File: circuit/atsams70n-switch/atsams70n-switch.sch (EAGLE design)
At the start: 70 parts, among them J5 CONN_20X2, Q1 20MHz, U1 REGULATOR_SOT223, U2 ATSAMS70N-TQFP100, U3 ISL3177E, U4 ISL3177E, U5 ISL3177E, U6 ISL3177E, X1 MICRO-USB_1/100

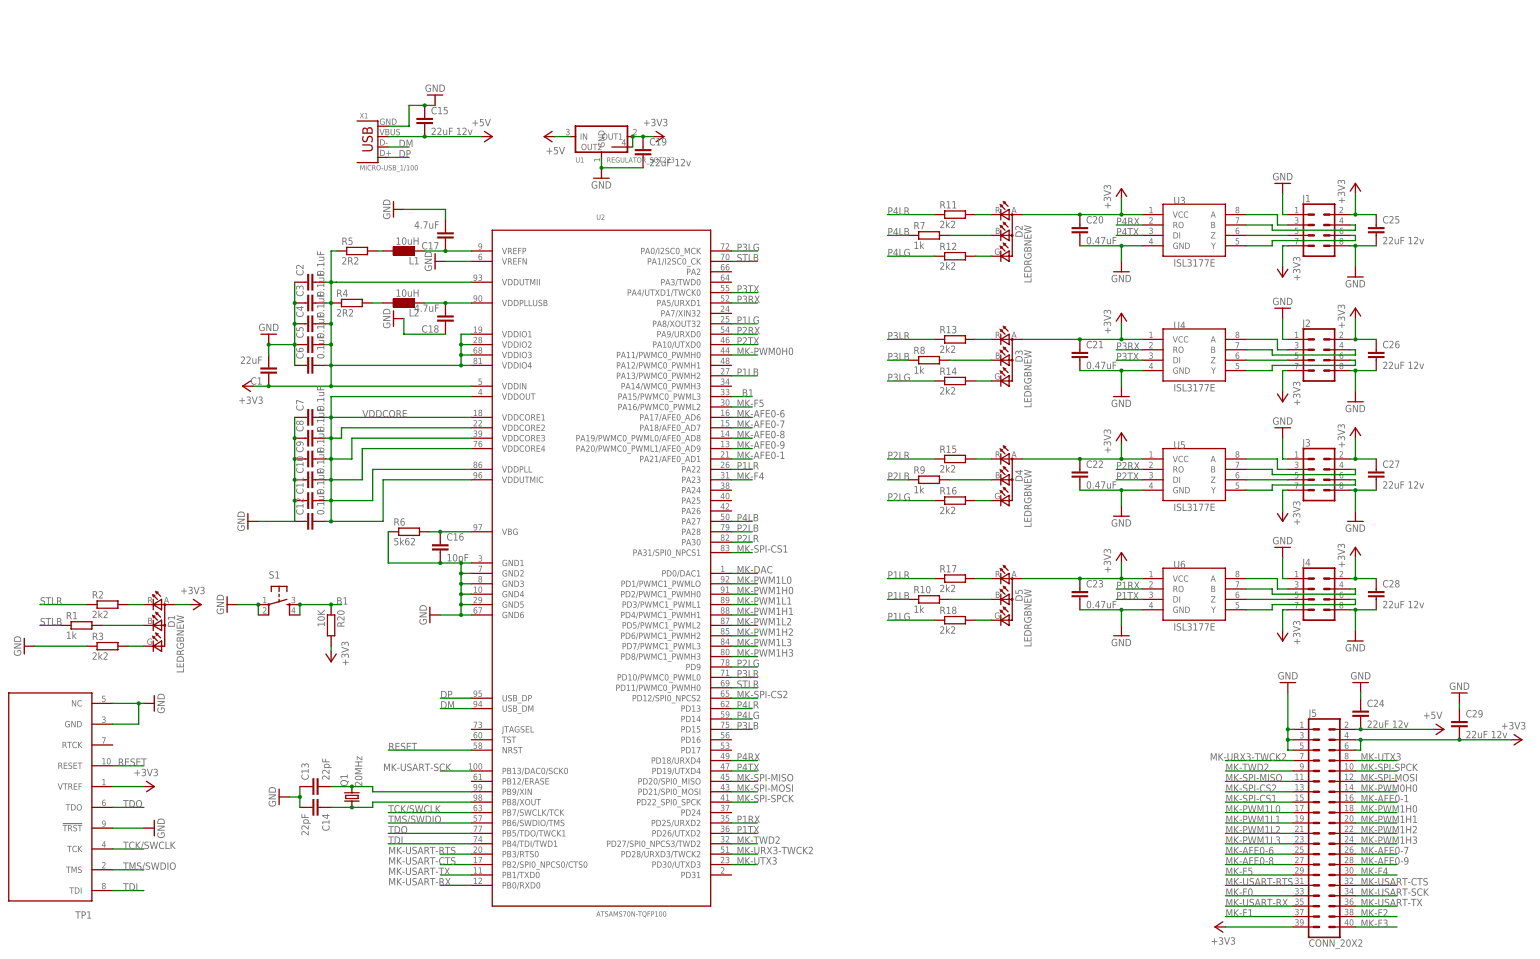
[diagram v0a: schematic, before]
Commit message: new boards to house
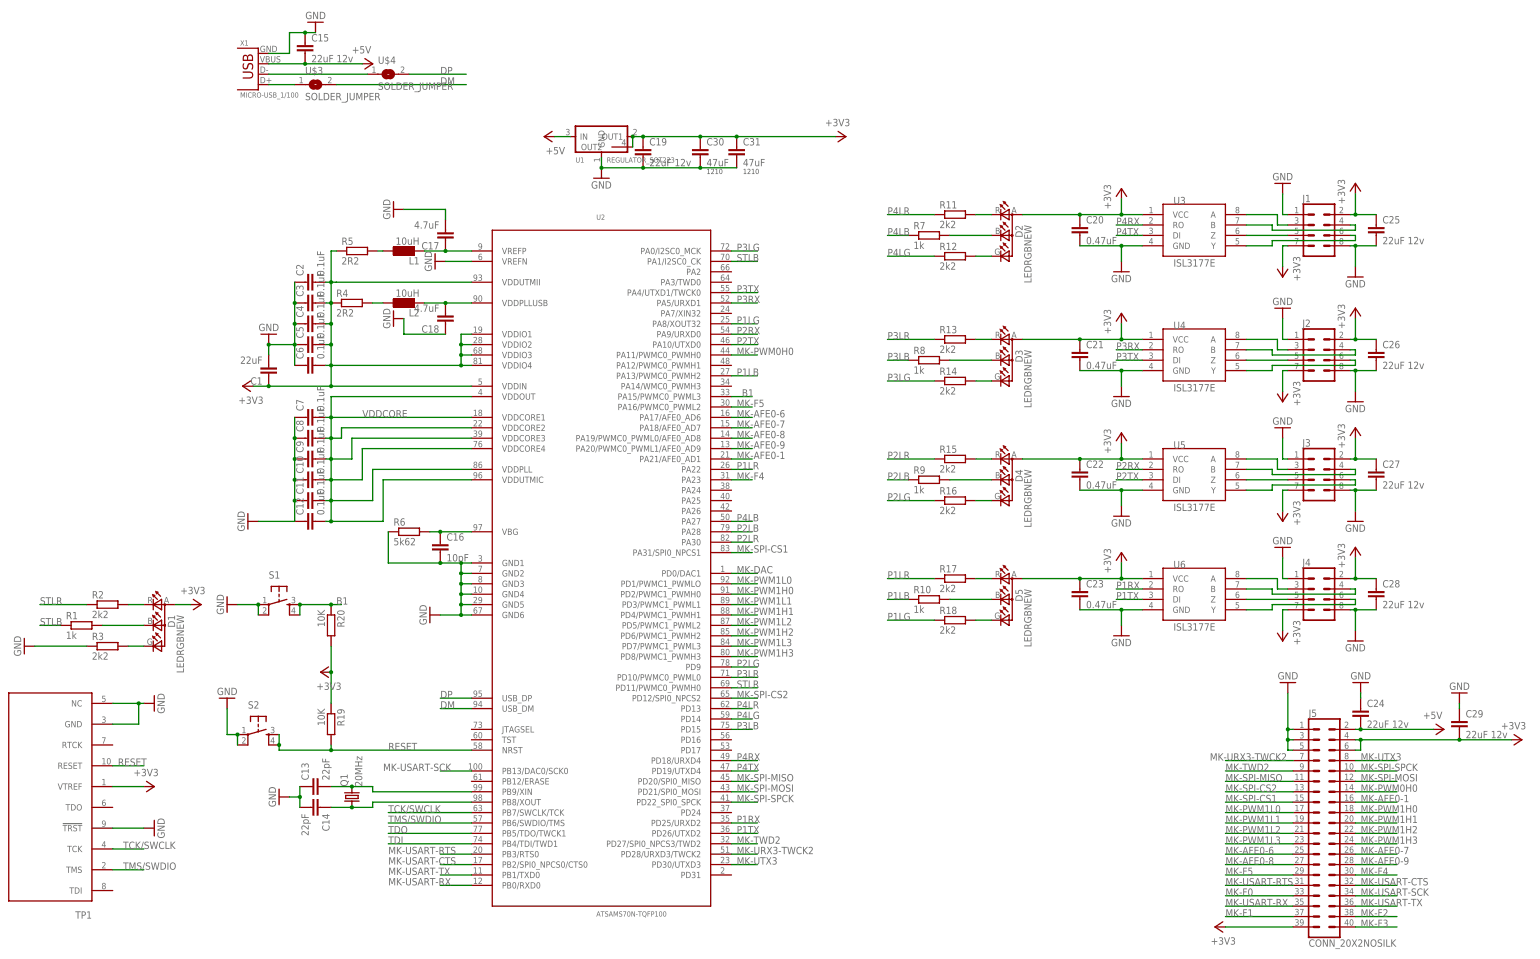
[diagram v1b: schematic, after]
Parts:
- added C30, C31: 47uF, borkedlabs-passives:CAP1210
- added R19: 10K, eagle-ltspice:R
- added S2: (no value), fab:6MM_SWITCH6MM_SWITCH
- added U$3, U$4: SOLDER_JUMPER, fab:SOLDER_JUMPER
- J5: value CONN_20X2 -> CONN_20X2NOSILK; device SparkFun-Connectors:CONN_20X2 -> SparkFun-Connectors:CONN_20X2NOSILK
- TP1: value TC2050-MCP-NL -> TC2050-NL; device tag-connect-2050:TC2050-MCP-NL -> tag-connect-2050:TC2050-NL
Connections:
- new net N$40: U$3.1, X1.D+
- new net N$6: U$4.1, X1.D-
- net +3V3: now also C30.1, C31.1, R19.1
- net DM: now also U$3.2; no longer X1.D-
- net DP: now also U$4.2; no longer X1.D+
- net GND: now also C30.2, C31.2, S2.P, S2.P1
- net RESET: now also R19.2, S2.S, S2.S1
- net TDI: no longer TP1.TDI
- net TDO: no longer TP1.TDO
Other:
- moved on the sheet: C15, X1

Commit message: new hardware
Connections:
- net MK-DAC: now also U2.PD0/DAC1/PWMC1_PWML0; no longer U2.PD0/DAC1
- net MK-PWM1H0: now also U2.PD2/PWMC1_PWML1; no longer U2.PD2/PWMC1_PWMH0
- net MK-PWM1H1: now also U2.PD4/PWMC1_PWML2; no longer U2.PD4/PWMC1_PWMH1
- net MK-PWM1H2: now also U2.PD6/PWMC1_PWML3; no longer U2.PD6/PWMC1_PWMH2
- net MK-PWM1H3: now also U2.PD8; no longer U2.PD8/PWMC1_PWMH3
- net MK-PWM1L0: now also U2.PD1/PWMC1_PWMH0; no longer U2.PD1/PWMC1_PWMLO
- net MK-PWM1L1: now also U2.PD3/PWMC1_PWMH1; no longer U2.PD3/PWMC1_PWML1
- net MK-PWM1L2: now also U2.PD5/PWMC1_PWMH2; no longer U2.PD5/PWMC1_PWML2
- net MK-PWM1L3: now also U2.PD7/PWMC1_PWMH3; no longer U2.PD7/PWMC1_PWML3
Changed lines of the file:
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@@
 <grid distance="0.05" unitdist="inch" unit="inch" style="lines" multiple="1" display="yes" altdistance="0.01" altunitdist="inch" altunit="inch"/>
 <layers>
-<layer number="1" name="Top" color="4" fill="1" visible="yes" active="no"/>
-<layer number="16" name="Bottom" color="1" fill="1" visible="yes" active="no"/>
-<layer number="17" name="Pads" color="2" fill="1" visible="yes" active="no"/>
-<layer number="18" name="Vias" color="2" fill="1" visible="yes" active="no"/>
-<layer number="19" name="Unrouted" color="6" fill="1" visible="yes" active="no"/>
-<layer number="20" name="Dimension" color="24" fill="1" visible="yes" active="no"/>
-<layer number="21" name="tPlace" color="7" fill="1" visible="yes" active="no"/>
-<layer number="22" name="bPlace" color="7" fill="1" visible="yes" active="no"/>
-<layer number="23" name="tOrigins" color="15" fill="1" visible="yes" active="no"/>
-<layer number="24" name="bOrigins" color="15" fill="1" visible="yes" active="no"/>
-<layer number="25" name="tNames" color="7" fill="1" visible="yes" active="no"/>
-<layer number="26" name="bNames" color="7" fill="1" visible="yes" active="no"/>
-<layer number="27" name="tValues" color="7" fill="1" visible="yes" active="no"/>
-<layer number="28" name="bValues" color="7" fill="1" visible="yes" active="no"/>
+<layer number="1" name="Top" color="4" fill="1" visible="no" active="no"/>
+<layer number="16" name="Bottom" color="1" fill="1" visible="no" active="no"/>
+<layer number="17" name="Pads" color="2" fill="1" visible="no" active="no"/>
+<layer number="18" name="Vias" color="2" fill="1" visible="no" active="no"/>
+<layer number="19" name="Unrouted" color="6" fill="1" visible="no" active="no"/>
+<layer number="20" name="Dimension" color="24" fill="1" visible="no" active="no"/>
+<layer number="21" name="tPlace" color="7" fill="1" visible="no" active="no"/>
+<layer number="22" name="bPlace" color="7" fill="1" visible="no" active="no"/>
+<layer number="23" name="tOrigins" color="15" fill="1" visible="no" active="no"/>
+<layer number="24" name="bOrigins" color="15" fill="1" visible="no" active="no"/>
+<layer number="25" name="tNames" color="7" fill="1" visible="no" active="no"/>
+<layer number="26" name="bNames" color="7" fill="1" visible="no" active="no"/>
+<layer number="27" name="tValues" color="7" fill="1" visible="no" active="no"/>
+<layer number="28" name="bValues" color="7" fill="1" visible="no" active="no"/>
 <layer number="29" name="tStop" color="7" fill="3" visible="no" active="no"/>
 <layer number="30" name="bStop" color="7" fill="6" visible="no" active="no"/>
@@
 <layer number="35" name="tGlue" color="7" fill="4" visible="no" active="no"/>
 <layer number="36" name="bGlue" color="7" fill="5" visible="no" active="no"/>
-<layer number="37" name="tTest" color="7" fill="1" visible="yes" active="no"/>
-<layer number="38" name="bTest" color="7" fill="1" visible="yes" active="no"/>
+<layer number="37" name="tTest" color="7" fill="1" visible="no" active="no"/>
+<layer number="38" name="bTest" color="7" fill="1" visible="no" active="no"/>
 <layer number="39" name="tKeepout" color="4" fill="11" visible="no" active="no"/>
 <layer number="40" name="bKeepout" color="1" fill="11" visible="no" active="no"/>
@@
 <layer number="44" name="Drills" color="7" fill="1" visible="no" active="no"/>
 <layer number="45" name="Holes" color="7" fill="1" visible="no" active="no"/>
-<layer number="46" name="Milling" color="3" fill="1" visible="yes" active="no"/>
-<layer number="47" name="Measures" color="7" fill="1" visible="yes" active="no"/>
-<layer number="48" name="Document" color="7" fill="1" visible="yes" active="no"/>
-<layer number="49" name="Reference" color="7" fill="1" visible="yes" active="no"/>
-<layer number="50" name="dxf" color="7" fill="1" visible="yes" active="no"/>
-<layer number="51" name="tDocu" color="7" fill="1" visible="yes" active="no"/>
-<layer number="52" name="bDocu" color="7" fill="1" visible="yes" active="no"/>
-<layer number="53" name="tGND_GNDA" color="7" fill="9" visible="yes" active="no"/>
-<layer number="54" name="bGND_GNDA" color="1" fill="9" visible="yes" active="no"/>
-<layer number="56" name="wert" color="7" fill="1" visible="yes" active="no"/>
-<layer number="57" name="tCAD" color="7" fill="1" visible="yes" active="no"/>
-<layer number="59" name="tCarbon" color="7" fill="1" visible="yes" active="no"/>
-<layer number="60" name="bCarbon" color="7" fill="1" visible="yes" active="no"/>
+<layer number="46" name="Milling" color="3" fill="1" visible="no" active="no"/>
+<layer number="47" name="Measures" color="7" fill="1" visible="no" active="no"/>
+<layer number="48" name="Document" color="7" fill="1" visible="no" active="no"/>
+<layer number="49" name="Reference" color="7" fill="1" visible="no" active="no"/>
+<layer number="50" name="dxf" color="7" fill="1" visible="no" active="no"/>
+<layer number="51" name="tDocu" color="7" fill="1" visible="no" active="no"/>
+<layer number="52" name="bDocu" color="7" fill="1" visible="no" active="no"/>
+<layer number="53" name="tGND_GNDA" color="7" fill="9" visible="no" active="no"/>
+<layer number="54" name="bGND_GNDA" color="1" fill="9" visible="no" active="no"/>
+<layer number="56" name="wert" color="7" fill="1" visible="no" active="no"/>
+<layer number="57" name="tCAD" color="7" fill="1" visible="no" active="no"/>
+<layer number="59" name="tCarbon" color="7" fill="1" visible="no" active="no"/>
+<layer number="60" name="bCarbon" color="7" fill="1" visible="no" active="no"/>
 <layer number="90" name="Modules" color="5" fill="1" visible="yes" active="yes"/>
 <layer number="91" name="Nets" color="2" fill="1" visible="yes" active="yes"/>
@@
 <net name="MK-DAC" class="0">
 <segment>
-<pinref part="U2" gate="G$1" pin="PD0/DAC1"/>
+<pinref part="U2" gate="G$1" pin="PD0/DAC1/PWMC1_PWML0"/>
 <wire x1="88.9" y1="71.12" x2="95.25" y2="71.12" width="0.1524" layer="91"/>
 <label x="90.17" y="71.12" size="1.778" layer="95"/>
@@
 <net name="MK-PWM1L0" class="0">
 <segment>
-<pinref part="U2" gate="G$1" pin="PD1/PWMC1_PWMLO"/>
+<pinref part="U2" gate="G$1" pin="PD1/PWMC1_PWMH0"/>
 <wire x1="88.9" y1="68.58" x2="95.25" y2="68.58" width="0.1524" layer="91"/>
 <label x="90.17" y="68.58" size="1.778" layer="95"/>
@@
 </segment>
 <segment>
-<pinref part="U2" gate="G$1" pin="PD2/PWMC1_PWMH0"/>
+<pinref part="U2" gate="G$1" pin="PD2/PWMC1_PWML1"/>
 <wire x1="88.9" y1="66.04" x2="95.25" y2="66.04" width="0.1524" layer="91"/>
 <label x="90.17" y="66.04" size="1.778" layer="95"/>
@@
 </segment>
 <segment>
-<pinref part="U2" gate="G$1" pin="PD3/PWMC1_PWML1"/>
+<pinref part="U2" gate="G$1" pin="PD3/PWMC1_PWMH1"/>
 <wire x1="88.9" y1="63.5" x2="95.25" y2="63.5" width="0.1524" layer="91"/>
 <label x="90.17" y="63.5" size="1.778" layer="95"/>
@@
 </segment>
 <segment>
-<pinref part="U2" gate="G$1" pin="PD4/PWMC1_PWMH1"/>
+<pinref part="U2" gate="G$1" pin="PD4/PWMC1_PWML2"/>
 <wire x1="88.9" y1="60.96" x2="95.25" y2="60.96" width="0.1524" layer="91"/>
 <label x="90.17" y="60.96" size="1.778" layer="95"/>
@@
 </segment>
 <segment>
-<pinref part="U2" gate="G$1" pin="PD5/PWMC1_PWML2"/>
+<pinref part="U2" gate="G$1" pin="PD5/PWMC1_PWMH2"/>
 <wire x1="88.9" y1="58.42" x2="95.25" y2="58.42" width="0.1524" layer="91"/>
 <label x="90.17" y="58.42" size="1.778" layer="95"/>
@@
 </segment>
 <segment>
-<pinref part="U2" gate="G$1" pin="PD6/PWMC1_PWMH2"/>
+<pinref part="U2" gate="G$1" pin="PD6/PWMC1_PWML3"/>
 <wire x1="88.9" y1="55.88" x2="95.25" y2="55.88" width="0.1524" layer="91"/>
 <label x="90.17" y="55.88" size="1.778" layer="95"/>
@@
 </segment>
 <segment>
-<pinref part="U2" gate="G$1" pin="PD7/PWMC1_PWML3"/>
+<pinref part="U2" gate="G$1" pin="PD7/PWMC1_PWMH3"/>
 <wire x1="88.9" y1="53.34" x2="95.25" y2="53.34" width="0.1524" layer="91"/>
 <label x="90.17" y="53.34" size="1.778" layer="95"/>
@@
 </segment>
 <segment>
-<pinref part="U2" gate="G$1" pin="PD8/PWMC1_PWMH3"/>
+<pinref part="U2" gate="G$1" pin="PD8"/>
 <wire x1="88.9" y1="50.8" x2="95.25" y2="50.8" width="0.1524" layer="91"/>
 <label x="90.17" y="50.8" size="1.778" layer="95"/>
@@
 </segment>
 </net>
+<net name="N$45" class="0">
+<segment>
+<wire x1="106.68" y1="67.31" x2="109.22" y2="67.31" width="0.1524" layer="91"/>
+<wire x1="109.22" y1="67.31" x2="109.22" y2="53.34" width="0.1524" layer="91"/>
+<wire x1="109.22" y1="53.34" x2="106.68" y2="53.34" width="0.1524" layer="91"/>
+</segment>
+</net>
